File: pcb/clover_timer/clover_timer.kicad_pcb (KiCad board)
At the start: 2 copper layers, 30 x 30 mm, 6 parts, among them IC1 PMS150G-S08, J1 CR2032_Plus, J2 CR2032_Minus, SW1 SW_Push, SW2 SW_Push

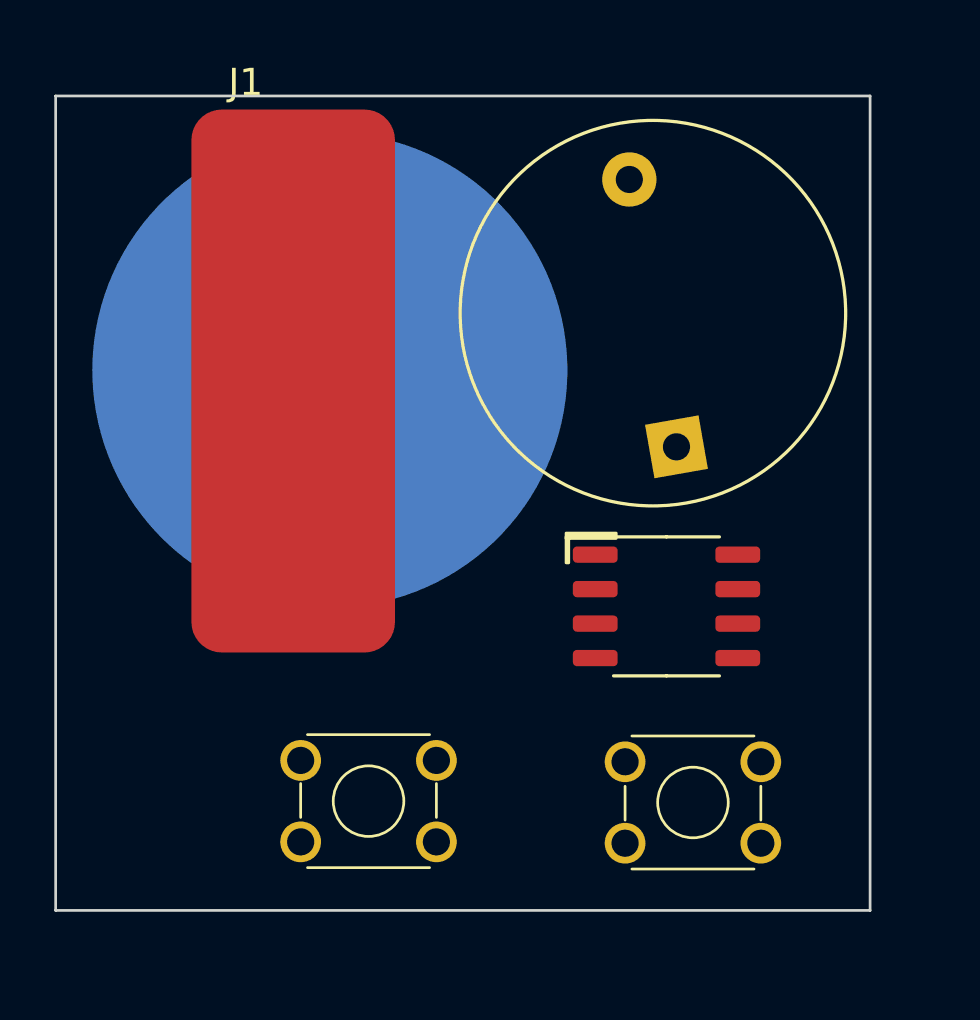
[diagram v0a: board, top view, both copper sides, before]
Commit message: update pcb, add docs
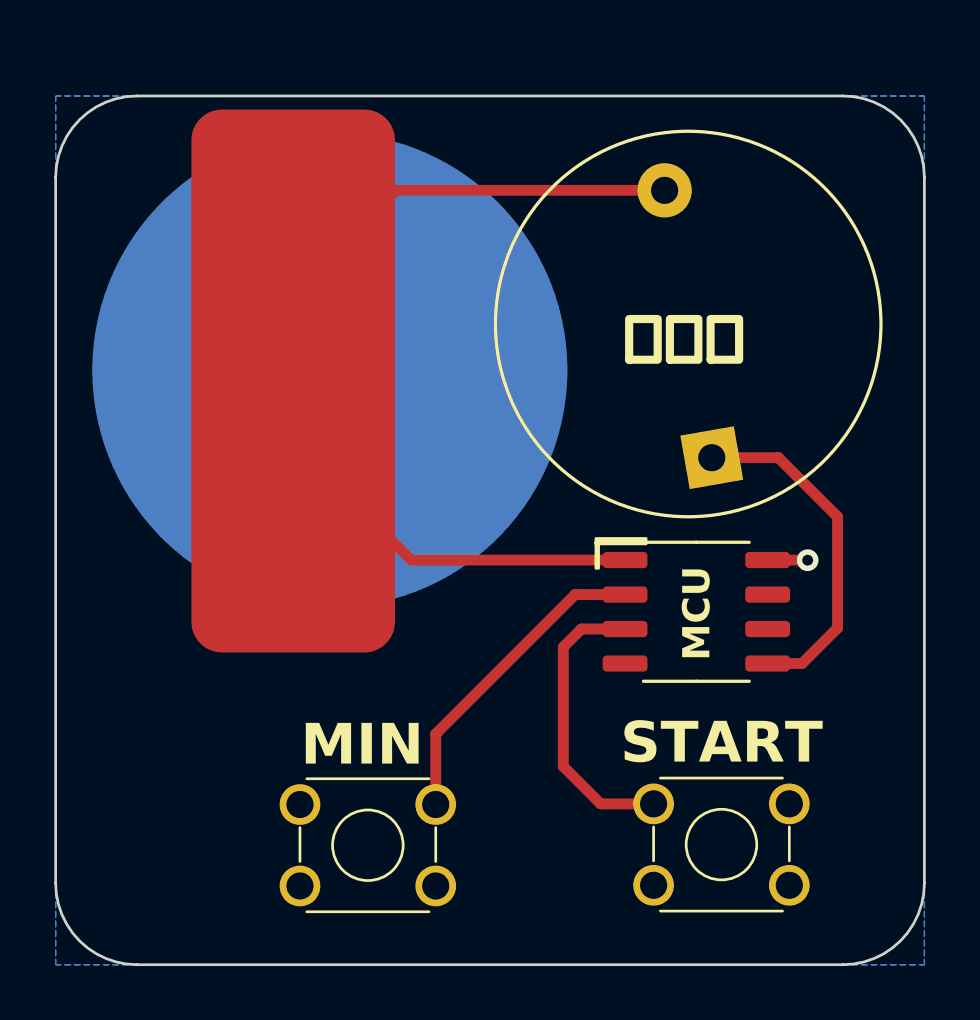
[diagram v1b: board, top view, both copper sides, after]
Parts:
- moved SW2 4.21 mm to (182.0, 96.1), turned to 0 degrees
- moved SW1 1.63 mm to (169.0, 96.1)
- moved BZ1 1.36 mm to (184.2, 83.3)
- moved IC1 1.12 mm to (183.6, 89.0)
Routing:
- net +3V0: track 0.00 -> 34.8 mm
- net Net-(BZ1--): track 0.00 -> 12.7 mm
- net Net-(IC1-PA7): track 0.00 -> 11.7 mm
- net Net-(IC1-PA6): track 0.00 -> 10.8 mm
- net GND: track 0.00 -> 1.48 mm, vias 0 -> 1
- added copper zone on B.Cu, net GND
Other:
- board size 30 x 30 mm -> 32 x 32 mm
- board text added: "MCU"
- board text added: "MIN"
- board text added: "START"
- board text added: "センサー街道 プロジェクト"
- board text added: "ブザー"
- board text removed: "センサー街道"
